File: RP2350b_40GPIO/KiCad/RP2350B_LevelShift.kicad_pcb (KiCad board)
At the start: 2 copper layers, 63.5 x 66.2 mm, 59 parts, among them J1 +5V, J10 SPI, J13 USB_B_Micro, J2 Right GPIO, J3 VGA, J4 Left GPIO, J7 SWD, J9 BOOT SEL, U1 LD1117S33TR_SOT223, U11 74CBTD3861, U12 74CBTD3861, U13 74CBTD3861, U14 74CBTD3861, U2 W25Q16JVSSIQ, U5 RP2350B-QFN80, U7 TLV74311PDBVR, Y1 12MHz

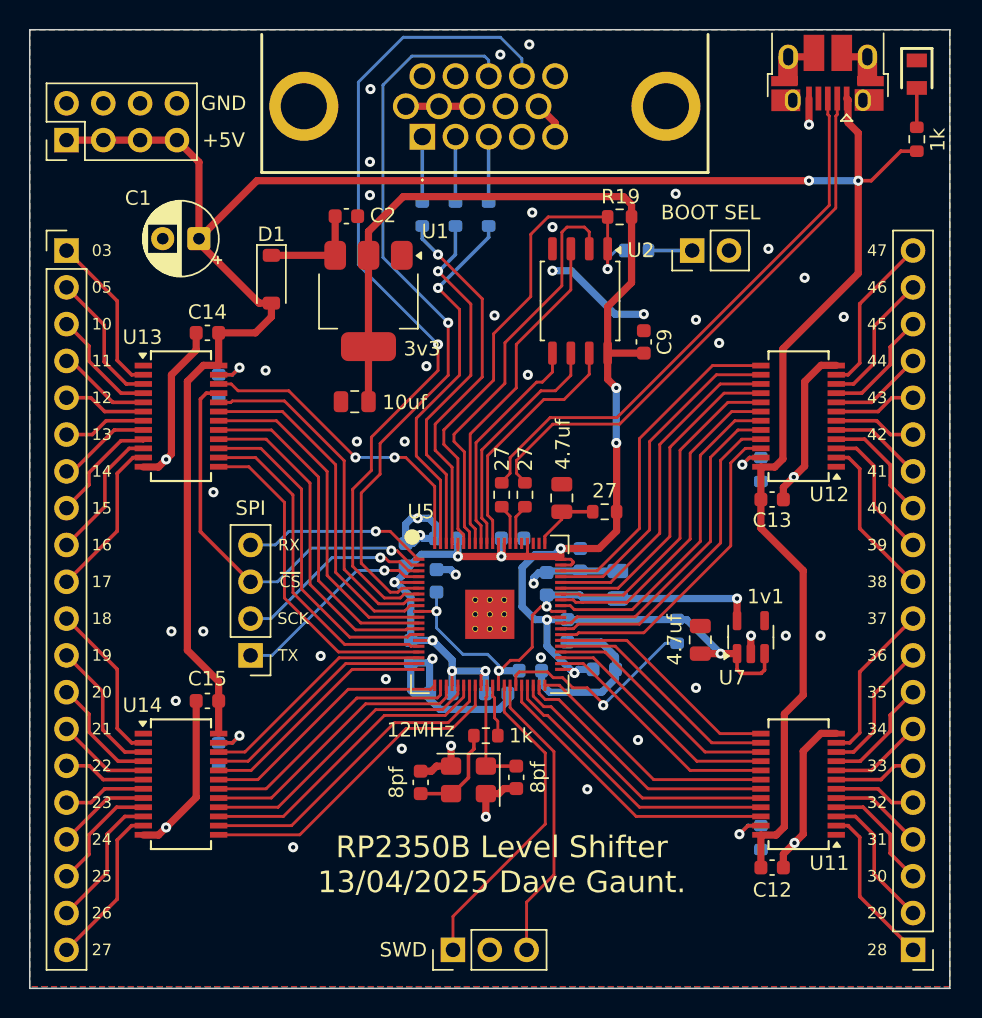
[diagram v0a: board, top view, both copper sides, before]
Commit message: - Updated To KiCad 10.0
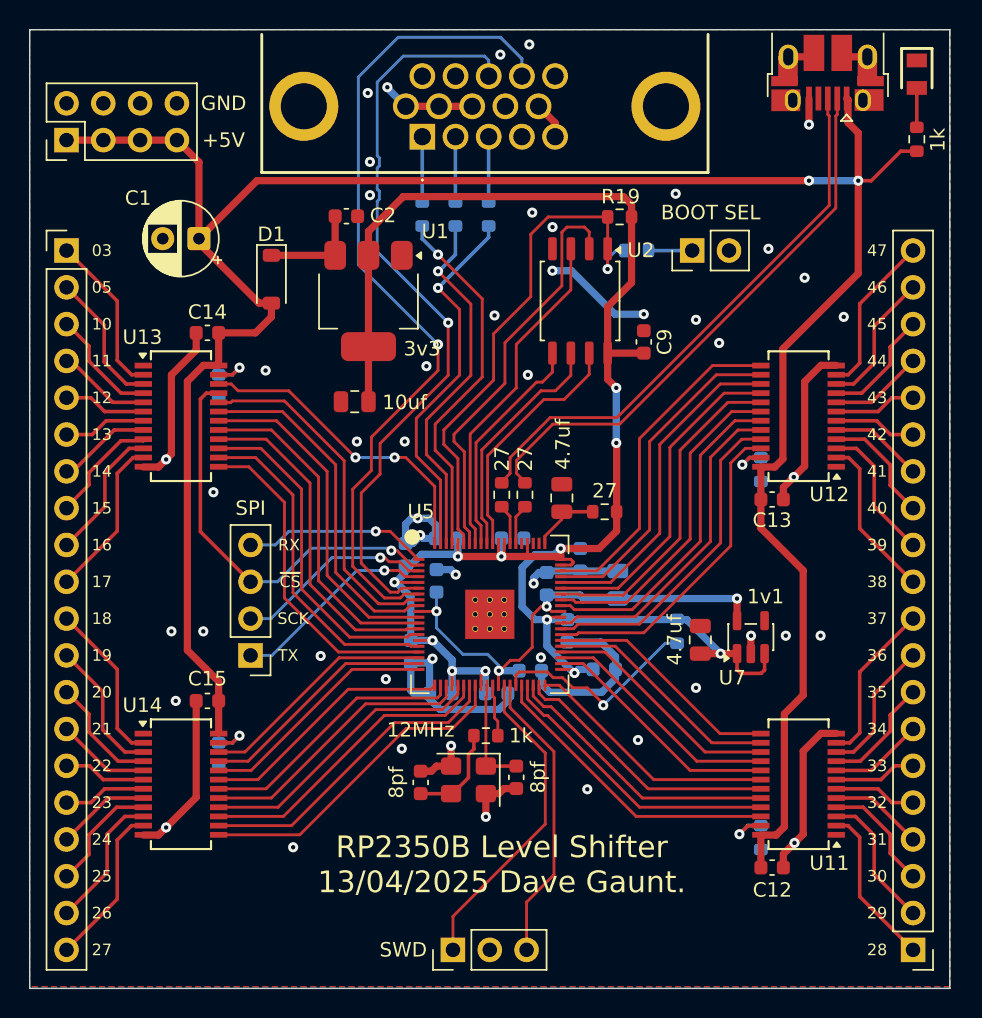
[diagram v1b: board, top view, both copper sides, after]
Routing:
- net GND: track 115.7 -> 128.8 mm, vias 48 -> 49
- net VGA_H_SYNC: track 51.6 -> 52.5 mm
